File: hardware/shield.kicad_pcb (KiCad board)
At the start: 2 copper layers, 101.6 x 53.3 mm, 12 parts, among them J1 Battery, P10 CONN_01X01, P11 CONN_01X01, P12 CONN_01X01, P2 Power, P3 Analog, P5 GPIO, P6 locked, P7 GPIO, P8 CONN_01X01, P9 CONN_01X01

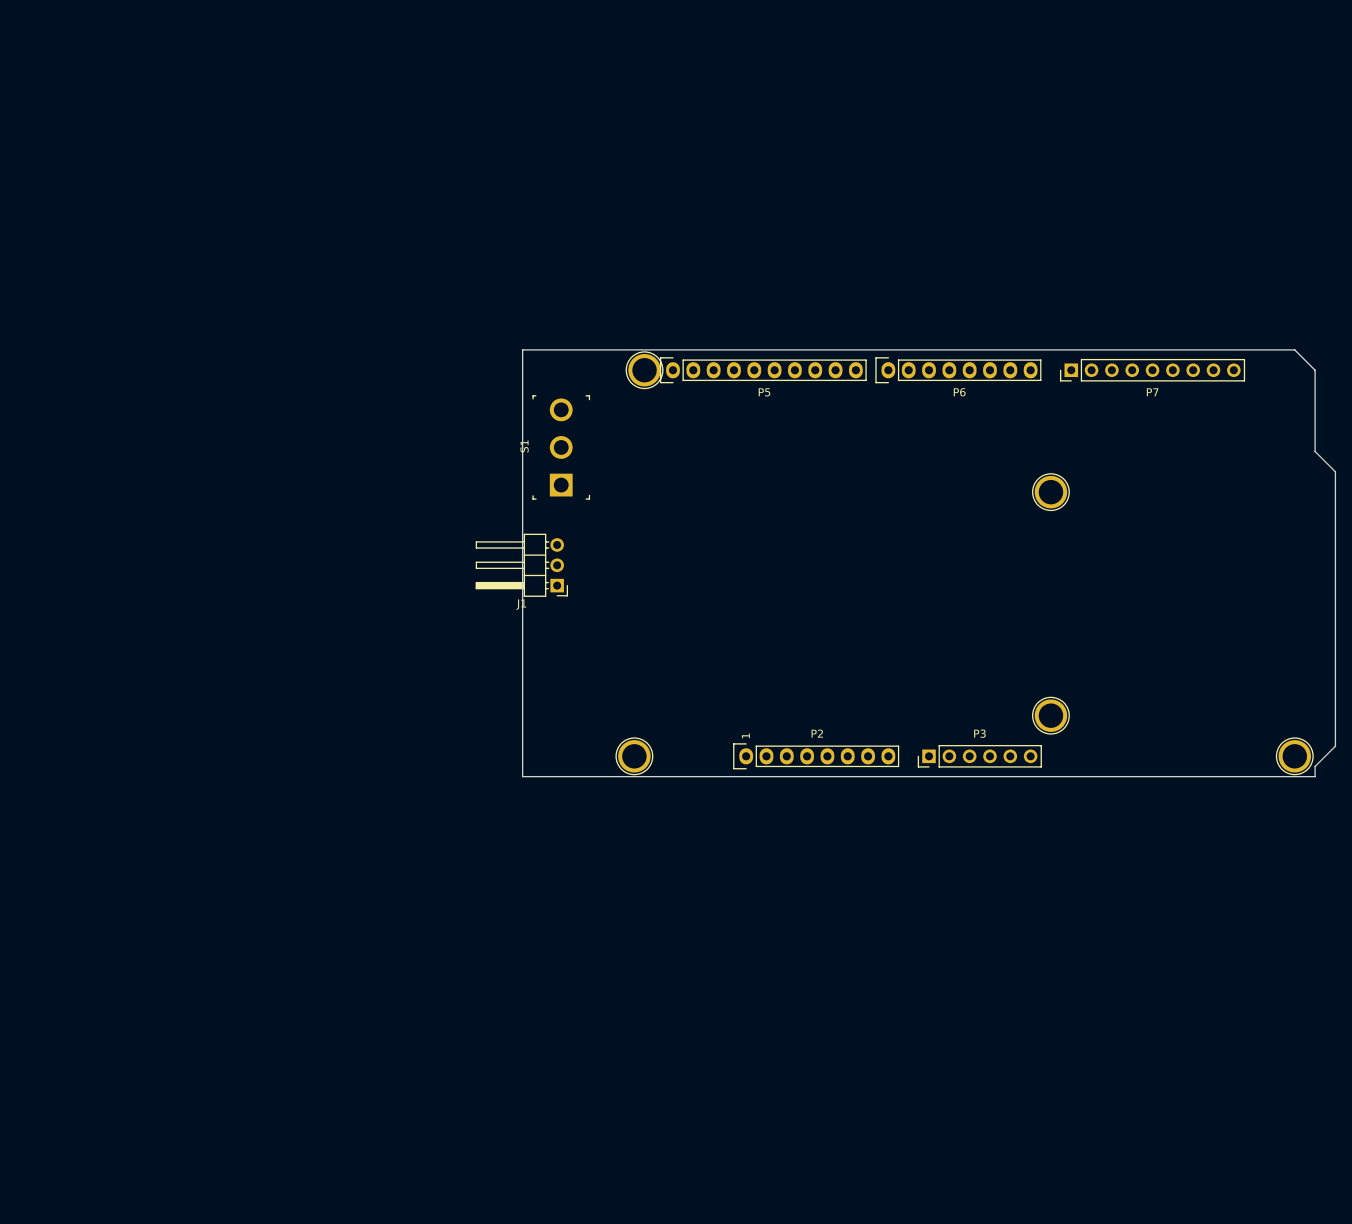
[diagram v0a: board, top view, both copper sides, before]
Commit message: First revision of the shield PCB
I have a few more tweaks that I would like to make before I send this
off to be manufactured. I ended up going with a 4 layer board as it has
signal wires going all over the place since I was a bit contrained with
part placement by most of the Arduino signal pins being on the right
side of the board and wanting to place connectors on the side closest
to the part to which they connect.
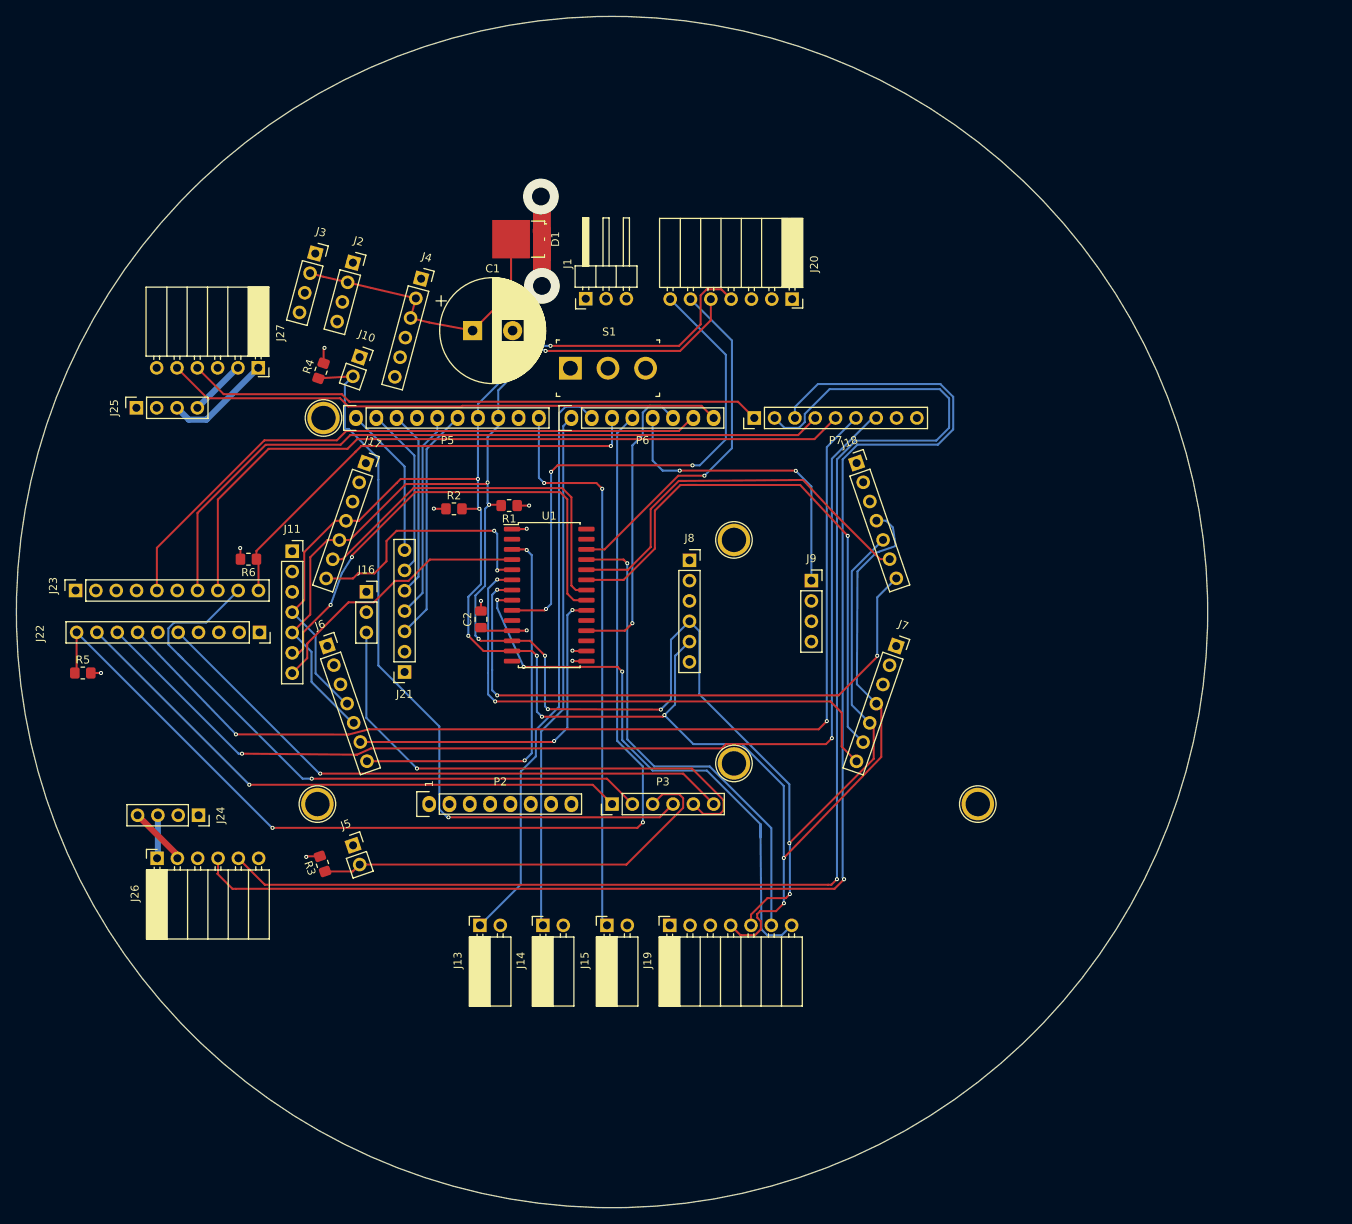
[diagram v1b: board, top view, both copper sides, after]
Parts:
- added C1: 2200uF 25V, Capacitor_THT:CP_Radial_D13.0mm_P5.00mm, F.Cu at (97.1, 65.9)
- added C2: 0.1uF, Capacitor_SMD:C_0805_2012Metric_Pad1.18x1.45mm_HandSolder, F.Cu at (98.2, 102.0)
- added D1: SS10P6-M3/86A, Package_TO_SOT_SMD:TO-277A, F.Cu at (103.0, 54.5)
- added J10: Right Photo Cell, Connector_PinSocket_2.54mm:PinSocket_1x02_P2.54mm_Vertical, F.Cu at (83.0, 69.2)
- added J11: Front Center Distance Sensor, Connector_PinSocket_2.54mm:PinSocket_1x07_P2.54mm_Vertical, F.Cu at (74.6, 93.5)
- added J13: Bumper Switch 1, Connector_PinSocket_2.54mm:PinSocket_1x02_P2.54mm_Horizontal, F.Cu at (98.0, 140.3)
- added J14: Bumper Switch 2, Connector_PinSocket_2.54mm:PinSocket_1x02_P2.54mm_Horizontal, F.Cu at (105.9, 140.3)
- added J15: Bumper Switch 3, Connector_PinSocket_2.54mm:PinSocket_1x02_P2.54mm_Horizontal, F.Cu at (113.9, 140.3)
- added J16: PIR Sensor, Connector_PinSocket_2.54mm:PinSocket_1x03_P2.54mm_Vertical, F.Cu at (83.8, 98.6)
- added J17: Front Right Distance Sensor, Connector_PinSocket_2.54mm:PinSocket_1x07_P2.54mm_Vertical, F.Cu at (83.8, 82.5)
- added J18: Back Right Distance Sensor, Connector_PinSocket_2.54mm:PinSocket_1x07_P2.54mm_Vertical, F.Cu at (145.1, 82.5)
- added J19: Left Cliff Sensor, Connector_PinSocket_2.54mm:PinSocket_1x07_P2.54mm_Horizontal, F.Cu at (121.8, 140.3)
- added J2: 3.3V 500mA Regulator, Connector_PinSocket_2.54mm:PinSocket_1x04_P2.54mm_Vertical, F.Cu at (82.2, 57.4)
- added J20: Right Cliff Sensor, Connector_PinSocket_2.54mm:PinSocket_1x07_P2.54mm_Horizontal, F.Cu at (137.1, 62.0)
- added J21: OLED, Connector_PinSocket_2.54mm:PinSocket_1x07_P2.54mm_Vertical, F.Cu at (88.6, 108.6)
- added J22: LMotor-1, Connector_PinSocket_2.54mm:PinSocket_1x10_P2.54mm_Vertical, F.Cu at (70.5, 103.6)
- added J23: RMotor-1, Connector_PinSocket_2.54mm:PinSocket_1x10_P2.54mm_Vertical, F.Cu at (47.5, 98.4)
- added J24: LMotor-2, Connector_PinSocket_2.54mm:PinSocket_1x04_P2.54mm_Vertical, F.Cu at (62.9, 126.5)
- added J25: RMotor-2, Connector_PinSocket_2.54mm:PinSocket_1x04_P2.54mm_Vertical, F.Cu at (55.1, 75.6)
- added J26: LeftMotor Conn, Connector_PinSocket_2.54mm:PinSocket_1x06_P2.54mm_Horizontal, F.Cu at (57.7, 131.9)
- added J27: RightMotor Conn, Connector_PinSocket_2.54mm:PinSocket_1x06_P2.54mm_Horizontal, F.Cu at (70.3, 70.6)
- added J3: 5.0V 500mA Regulator, Connector_PinSocket_2.54mm:PinSocket_1x04_P2.54mm_Vertical, F.Cu at (77.5, 56.3)
- added J4: 12V Boost Regulator, Connector_PinSocket_2.54mm:PinSocket_1x06_P2.54mm_Vertical, F.Cu at (90.7, 59.4)
- added J5: Left Photo Cell, Connector_PinSocket_2.54mm:PinSocket_1x02_P2.54mm_Vertical, F.Cu at (82.2, 130.3)
- added J6: Front Left Distance Sensor, Connector_PinSocket_2.54mm:PinSocket_1x07_P2.54mm_Vertical, F.Cu at (79.0, 105.3)
- added J7: Back Left Distance Sensor, Connector_PinSocket_2.54mm:PinSocket_1x07_P2.54mm_Vertical, F.Cu at (150.1, 105.3)
- added J8: IMU-1, Connector_PinSocket_2.54mm:PinSocket_1x06_P2.54mm_Vertical, F.Cu at (124.2, 94.6)
- added J9: IMU-2, Connector_PinSocket_2.54mm:PinSocket_1x04_P2.54mm_Vertical, F.Cu at (139.5, 97.2)
- added R1: 1k, Resistor_SMD:R_0805_2012Metric_Pad1.20x1.40mm_HandSolder, F.Cu at (101.7, 87.8)
- added R2: 1k, Resistor_SMD:R_0805_2012Metric_Pad1.20x1.40mm_HandSolder, F.Cu at (94.8, 88.2)
- added R3: 10k, Resistor_SMD:R_0805_2012Metric_Pad1.20x1.40mm_HandSolder, F.Cu at (78.4, 132.6)
- added R4: 10k, Resistor_SMD:R_0805_2012Metric_Pad1.20x1.40mm_HandSolder, F.Cu at (78.2, 70.9)
- added R5: 10k, Resistor_SMD:R_0805_2012Metric_Pad1.20x1.40mm_HandSolder, F.Cu at (48.4, 108.7)
- added R6: 10k, Resistor_SMD:R_0805_2012Metric_Pad1.20x1.40mm_HandSolder, F.Cu at (69.1, 94.5)
- added U1: MCP23018, Package_SO:SOIC-28W_7.5x17.9mm_P1.27mm, F.Cu at (106.7, 99.0)
- S1: value 100SP1T1B4M2QE -> Power Switch
- moved P11 40.6 mm to (78.5, 76.8)
- moved P2 40.1 mm to (91.7, 125.1)
- moved P5 40.1 mm to (82.5, 76.8)
- moved P6 40.1 mm to (109.5, 76.8)
- moved P12 40.1 mm to (129.8, 92.1)
- moved P10 40.1 mm to (160.3, 125.1)
- moved P3 40.1 mm to (114.6, 125.1)
- moved P7 40.1 mm to (132.3, 76.8)
- moved P8 40.1 mm to (77.7, 125.1)
- moved P9 40.1 mm to (129.8, 120.0)
- moved J1 36.0 mm to (111.3, 61.9), turned to 90 degrees
- moved S1 14.7 mm to (109.3, 70.6), turned to 0 degrees
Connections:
- net Net-(J1-Pad2) renamed VCC
- net VDD renamed +3V3
- P2 pad 5: +5V -> unconnected-(P2-Pad5)
- P3 pad 1: /P0.3 -> LMOTOR_OCM
- P3 pad 2: /P0.4 -> RMOTOR_OCM
- P3 pad 3: /P0.28 -> LPHOTO
- P3 pad 4: /P0.29 -> RPHOTO
- P3 pad 5: /P0.30 -> PIR_ALARM
- P3 pad 6: /P0.31 -> LMOTOR_EN
- P5 pad 1: /P0.27 -> OLED_CS
- P5 pad 10: /P0.19 -> BUMPERSW3
- P5 pad 2: /P0.26 -> OLED_DC
- P5 pad 3: /P0.2 -> OLED_RESET
- P5 pad 5: /P0.25 -> OLED_MOSI
- P5 pad 6: /P0.24 -> OLED_CLK
- P5 pad 7: /P0.23 -> I2C_SDA
- P5 pad 8: /P0.22 -> I2C_SCL
- P5 pad 9: /P0.20 -> unconnected-(P5-Pad9)
- P6 pad 1: /P0.18 -> BUMPERSW2
- P6 pad 2: /P0.17 -> BUMPERSW1
- P6 pad 3: /P0.16 -> RMOTOR_DIAG
- P6 pad 4: /P0.15 -> LMOTOR_DIAG
- P6 pad 5: /P0.14 -> IMU_INT
- P6 pad 6: /P0.13 -> SENSOR_INT
- P6 pad 7: /P0.12 -> RMOTOR_EN
- P6 pad 8: /P0.11 -> RMOTOR_ENC_B
- P7 pad 1: /P0.10 -> RMOTOR_ENC_A
- P7 pad 2: /P0.9 -> LMOTOR_ENC_B
- P7 pad 3: /P0.8 -> LMOTOR_ENC_A
- P7 pad 4: /P0.7 -> RMOTOR_PWM2
- P7 pad 5: /P0.6 -> RMOTOR_PWM1
- P7 pad 6: /P0.5 -> LMOTOR_PWM2
- P7 pad 7: /P0.21 -> LMOTOR_PWM1
- P7 pad 8: /P0.1 -> unconnected-(P7-Pad8)
- P7 pad 9: /P0.0 -> unconnected-(P7-Pad9)
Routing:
- net I2C_SDA: track 0.00 -> 259.4 mm, vias 0 -> 9
- net I2C_SCL: track 0.00 -> 252.2 mm, vias 0 -> 9
- net LMOTOR_ENC_A: track 0.00 -> 176.6 mm, vias 0 -> 1
- net LMOTOR_ENC_B: track 0.00 -> 173.7 mm, vias 0 -> 1
- net +BATT: track 0.00 -> 156.5 mm, vias 0 -> 2
- net LMOTOR_DIAG: track 0.00 -> 139.0 mm, vias 0 -> 2
- net LMOTOR_PWM1: track 0.00 -> 138.9 mm, vias 0 -> 2
- net LMOTOR_PWM2: track 0.00 -> 131.5 mm, vias 0 -> 2
- net RPHOTO: track 0.00 -> 94.3 mm, vias 0 -> 1
- net RMOTOR_PWM1: track 0.00 -> 92.8 mm
- net RMOTOR_PWM2: track 0.00 -> 91.8 mm
- net RMOTOR_OCM: track 0.00 -> 79.6 mm, vias 0 -> 1
- net RMOTOR_EN: track 0.00 -> 79.1 mm
- net LMOTOR_EN: track 0.00 -> 75.8 mm, vias 0 -> 1
- net /Sensors/BR_GPIO1: track 0.00 -> 75.8 mm, vias 0 -> 3
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- added copper zone on In2.Cu, net +3V3
- added copper zone on In1.Cu, net GND
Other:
- board size 101.6 x 53.3 mm -> 148.9 x 148.9 mm
- copper layers 2 -> 4
- rule pad_to_mask_clearance: 0 -> 0.0508

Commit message: Cleanup PCB layout
* Made the board outline a bit smaller.
* Added the 3D .step files for all of the parts that I could find. This
  was all the parts except for the IMU from Adafruit.
* Fixed an issue where I had the back distance sensors facing in the
  wrong direction.
* Added CC BY-SA licensing info for the KiCad design files.
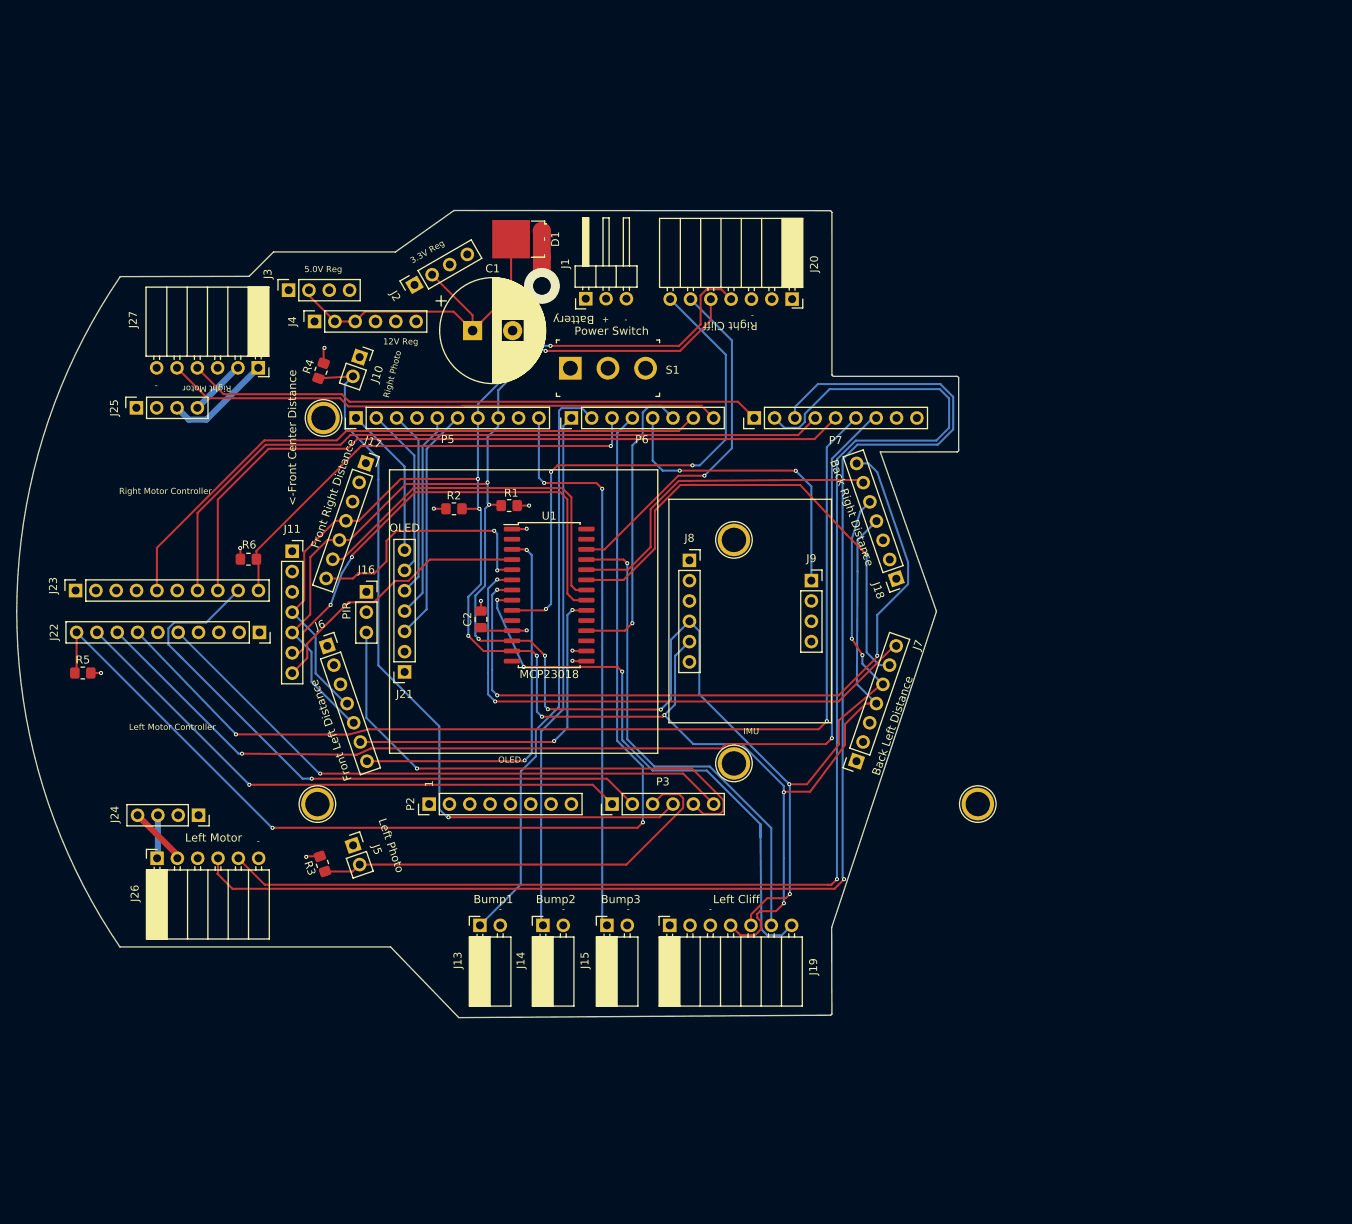
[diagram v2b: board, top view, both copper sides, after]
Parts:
- J11: value Front Center Distance Sensor -> <-Front Center Distance
- J13: value Bumper Switch 1 -> Bump1
- J14: value Bumper Switch 2 -> Bump2
- J15: value Bumper Switch 3 -> Bump3
- J16: value PIR Sensor -> PIR
- J17: value Front Right Distance Sensor -> Front Right Distance
- J18: value Back Right Distance Sensor -> Back Right Distance
- J19: value Left Cliff Sensor -> Left Cliff
- J20: value Right Cliff Sensor -> Right Cliff
- J26: value LeftMotor Conn -> Left Motor
- J5: value Left Photo Cell -> Left Photo
- J6: value Front Left Distance Sensor -> Front Left Distance
- J7: value Back Left Distance Sensor -> Back Left Distance
- P2: footprint Socket_Arduino_Mega:Socket_Strip_Arduino_1x08 -> Connector_PinHeader_2.54mm:PinHeader_1x08_P2.54mm_Vertical
- P5: footprint Socket_Arduino_Mega:Socket_Strip_Arduino_1x10 -> Connector_PinHeader_2.54mm:PinHeader_1x10_P2.54mm_Vertical
- P6: value locked -> GPIO; footprint Socket_Arduino_Mega:Socket_Strip_Arduino_1x08 -> Connector_PinHeader_2.54mm:PinHeader_1x08_P2.54mm_Vertical
- moved J18 15.3 mm to (150.1, 96.9), turned to -161 degrees
- moved J7 15.2 mm to (145.1, 119.7), turned to 161 degrees
- moved J4 14.4 mm to (77.4, 64.8), turned to 90 degrees
- moved J2 8.19 mm to (89.9, 60.2), turned to 120 degrees
- moved J3 5.66 mm to (74.1, 60.9), turned to 90 degrees
- turned P2 to 90 degrees
- turned P5 to 90 degrees
- turned P6 to 90 degrees
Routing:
- net /Sensors/BR_GPIO1: track 75.8 -> 93.3 mm
- net Net-(C1-Pad1): track 37.5 -> 46.5 mm
- net I2C_SDA: track 259.4 -> 250.5 mm
- net +5V: track 59.2 -> 67.0 mm
- net /Sensors/BL_XSHUT: track 71.2 -> 63.7 mm
- net /Sensors/BR_XSHUT: track 50.0 -> 42.6 mm
- net +12V: track 29.6 -> 36.4 mm
- net +BATT: track 156.5 -> 149.9 mm, vias 2 -> 1
- net /Sensors/BL_GPIO1: track 68.7 -> 70.9 mm
- net I2C_SCL: track 252.2 -> 250.9 mm, vias 9 -> 11
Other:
- board size 148.9 x 148.9 mm -> 117.7 x 100.9 mm
- board text added: "+"
- board text added: "-"
- board text added: "12V Reg"
- board text added: "3.3V Reg"
- board text added: "5.0V Reg"
- board text added: "IMU"
- board text added: "Left Motor Controller"
- board text added: "OLED"
- board text added: "Right Motor"
- board text added: "Right Motor Controller"
- board text added: "Right Photo"
- board text added: "https://github.com/adamgreen/rugrover"
